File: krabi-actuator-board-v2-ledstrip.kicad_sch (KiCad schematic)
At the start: 0 parts

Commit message: adding LED strip
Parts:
- added LS1, LS2: Conn_01x02_Pin, symbol Connector:Conn_01x02_Pin
- added Q_LS1, Q_LS2: Q_NPN_BCE, symbol Device:Q_NPN_BCE
- added RB_LS1, RB_LS2: 1.2k, Resistor_SMD:R_0805_2012Metric, symbol Device:R
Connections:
- new net: LS2.1 (Pin_1), Q_LS2.2 (C)
- new net: Q_LS1.1 (B), RB_LS1.2
- new net: Q_LS2.1 (B), RB_LS2.2
- new net: LS1.1 (Pin_1), Q_LS1.2 (C)
- new net 12V: LS1.2 (Pin_2), LS2.2 (Pin_2)
- new net GND: Q_LS1.3 (E), Q_LS2.3 (E)
- new net LEDS_1: RB_LS1.1
- new net LEDS_2: RB_LS2.1
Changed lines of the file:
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@@
 (kicad_sch (version 20230121) (generator eeschema)
   (paper "A4")
+  (wire (pts (xy 53.34 45.72) (xy 57.15 45.72))
+    (stroke (width 0) (type default))
+  )
+  (wire (pts (xy 82.55 35.56) (xy 82.55 40.64))
+    (stroke (width 0) (type default))
+  )
+  (wire (pts (xy 85.09 77.47) (xy 85.09 82.55))
+    (stroke (width 0) (type default))
+  )
+  (wire (pts (xy 78.74 29.21) (xy 78.74 33.02))
+    (stroke (width 0) (type default))
+  )
+  (wire (pts (xy 85.09 74.93) (xy 81.28 74.93))
+    (stroke (width 0) (type default))
+  )
+  (wire (pts (xy 85.09 92.71) (xy 85.09 96.52))
+    (stroke (width 0) (type default))
+  )
+  (wire (pts (xy 67.31 87.63) (xy 77.47 87.63))
+    (stroke (width 0) (type default))
+  )
+  (wire (pts (xy 55.88 87.63) (xy 59.69 87.63))
+    (stroke (width 0) (type default))
+  )
+  (wire (pts (xy 64.77 45.72) (xy 74.93 45.72))
+    (stroke (width 0) (type default))
+  )
+  (wire (pts (xy 81.28 71.12) (xy 81.28 74.93))
+    (stroke (width 0) (type default))
+  )
+  (wire (pts (xy 82.55 50.8) (xy 82.55 54.61))
+    (stroke (width 0) (type default))
+  )
+  (wire (pts (xy 82.55 33.02) (xy 78.74 33.02))
+    (stroke (width 0) (type default))
+  )
+  (global_label "GND" (shape input) (at 82.55 54.61 270) (fields_autoplaced)
+    (effects (font (size 1.27 1.27)) (justify right))
+    (property "Intersheetrefs" "${INTERSHEET_REFS}" (at 82.55 61.5608 90)
+      (effects (font (size 1.27 1.27)) (justify right) hide)
+    )
+  )
+  (global_label "12V" (shape input) (at 78.74 29.21 90) (fields_autoplaced)
+    (effects (font (size 1.27 1.27)) (justify left))
+    (property "Intersheetrefs" "${INTERSHEET_REFS}" (at 78.74 22.6221 90)
+      (effects (font (size 1.27 1.27)) (justify left) hide)
+    )
+  )
+  (global_label "LEDS_2" (shape input) (at 55.88 87.63 180) (fields_autoplaced)
+    (effects (font (size 1.27 1.27)) (justify right))
+    (property "Intersheetrefs" "${INTERSHEET_REFS}" (at 45.966 87.63 0)
+      (effects (font (size 1.27 1.27)) (justify right) hide)
+    )
+  )
+  (global_label "LEDS_1" (shape input) (at 53.34 45.72 180) (fields_autoplaced)
+    (effects (font (size 1.27 1.27)) (justify right))
+    (property "Intersheetrefs" "${INTERSHEET_REFS}" (at 43.426 45.72 0)
+      (effects (font (size 1.27 1.27)) (justify right) hide)
+    )
+  )
+  (global_label "GND" (shape input) (at 85.09 96.52 270) (fields_autoplaced)
+    (effects (font (size 1.27 1.27)) (justify right))
+    (property "Intersheetrefs" "${INTERSHEET_REFS}" (at 85.09 103.4708 90)
+      (effects (font (size 1.27 1.27)) (justify right) hide)
+    )
+  )
+  (global_label "12V" (shape input) (at 81.28 71.12 90) (fields_autoplaced)
+    (effects (font (size 1.27 1.27)) (justify left))
+    (property "Intersheetrefs" "${INTERSHEET_REFS}" (at 81.28 64.5321 90)
+      (effects (font (size 1.27 1.27)) (justify left) hide)
+    )
+  )
+  (symbol (lib_id "Connector:Conn_01x02_Pin") (at 90.17 77.47 180) (unit 1)
+    (in_bom yes) (on_board yes) (dnp no) (fields_autoplaced)
+    (property "Reference" "LS2" (at 91.44 74.93 0)
+      (effects (font (size 1.27 1.27)) (justify right))
+    )
+    (property "Value" "Conn_01x02_Pin" (at 91.44 77.47 0)
+      (effects (font (size 1.27 1.27)) (justify right))
+    )
+    (property "Footprint" "" (at 90.17 77.47 0)
+      (effects (font (size 1.27 1.27)) hide)
+    )
+    (property "Datasheet" "~" (at 90.17 77.47 0)
+      (effects (font (size 1.27 1.27)) hide)
+    )
+    (property "Sim.Enable" "0" (at 90.17 77.47 0)
+      (effects (font (size 1.27 1.27)) hide)
+    )
+    (pin "1")
+    (pin "2")
+    (instances
+      (project "krabi-actuator-board-v2"
+        (path "/e63e39d7-6ac0-4ffd-8aa3-1841a4541b55/55fd7014-48ef-4cf3-914d-288b69fed1ef"
+          (reference "LS2") (unit 1)
+        )
+      )
+    )
+  )
+  (symbol (lib_id "Device:R") (at 60.96 45.72 90) (unit 1)
+    (in_bom yes) (on_board yes) (dnp no) (fields_autoplaced)
+    (property "Reference" "RB_LS1" (at 60.96 39.37 90)
+      (effects (font (size 1.27 1.27)))
+    )
+    (property "Value" "1.2k" (at 60.96 41.91 90)
+      (effects (font (size 1.27 1.27)))
+    )
+    (property "Footprint" "Resistor_SMD:R_0805_2012Metric" (at 60.96 47.498 90)
+      (effects (font (size 1.27 1.27)))
+    )
+    (property "Datasheet" "~" (at 60.96 45.72 0)
+      (effects (font (size 1.27 1.27)) hide)
+    )
+    (pin "1")
+    (pin "2")
+    (instances
+      (project "krabi-actuator-board-v2"
+        (path "/e63e39d7-6ac0-4ffd-8aa3-1841a4541b55/55fd7014-48ef-4cf3-914d-288b69fed1ef"
+          (reference "RB_LS1") (unit 1)
+        )
+      )
+    )
+  )
+  (symbol (lib_id "Device:Q_NPN_BCE") (at 82.55 87.63 0) (unit 1)
+    (in_bom yes) (on_board yes) (dnp no) (fields_autoplaced)
+    (property "Reference" "Q_LS2" (at 87.63 86.36 0)
+      (effects (font (size 1.27 1.27)) (justify left))
+    )
+    (property "Value" "Q_NPN_BCE" (at 87.63 88.9 0)
+      (effects (font (size 1.27 1.27)) (justify left))
+    )
+    (property "Footprint" "" (at 87.63 85.09 0)
+      (effects (font (size 1.27 1.27)) hide)
+    )
+    (property "Datasheet" "~" (at 82.55 87.63 0)
+      (effects (font (size 1.27 1.27)) hide)
+    )
+    (property "Sim.Enable" "0" (at 82.55 87.63 0)
+      (effects (font (size 1.27 1.27)) hide)
+    )
+    (pin "1")
+    (pin "2")
+    (pin "3")
+    (instances
+      (project "krabi-actuator-board-v2"
+        (path "/e63e39d7-6ac0-4ffd-8aa3-1841a4541b55/55fd7014-48ef-4cf3-914d-288b69fed1ef"
+          (reference "Q_LS2") (unit 1)
+        )
+      )
+    )
+  )
+  (symbol (lib_id "Device:Q_NPN_BCE") (at 80.01 45.72 0) (unit 1)
+    (in_bom yes) (on_board yes) (dnp no) (fields_autoplaced)
+    (property "Reference" "Q_LS1" (at 85.09 44.45 0)
+      (effects (font (size 1.27 1.27)) (justify left))
+    )
+    (property "Value" "Q_NPN_BCE" (at 85.09 46.99 0)
+      (effects (font (size 1.27 1.27)) (justify left))
+    )
+    (property "Footprint" "" (at 85.09 43.18 0)
+      (effects (font (size 1.27 1.27)) hide)
+    )
+    (property "Datasheet" "~" (at 80.01 45.72 0)
+      (effects (font (size 1.27 1.27)) hide)
+    )
+    (property "Sim.Enable" "0" (at 80.01 45.72 0)
+      (effects (font (size 1.27 1.27)) hide)
+    )
+    (pin "1")
+    (pin "2")
+    (pin "3")
+    (instances
+      (project "krabi-actuator-board-v2"
+        (path "/e63e39d7-6ac0-4ffd-8aa3-1841a4541b55/55fd7014-48ef-4cf3-914d-288b69fed1ef"
+          (reference "Q_LS1") (unit 1)
+        )
+      )
+    )
+  )
+  (symbol (lib_id "Device:R") (at 63.5 87.63 90) (unit 1)
+    (in_bom yes) (on_board yes) (dnp no) (fields_autoplaced)
+    (property "Reference" "RB_LS2" (at 63.5 81.28 90)
+      (effects (font (size 1.27 1.27)))
+    )
+    (property "Value" "1.2k" (at 63.5 83.82 90)
+      (effects (font (size 1.27 1.27)))
+    )
+    (property "Footprint" "Resistor_SMD:R_0805_2012Metric" (at 63.5 89.408 90)
+      (effects (font (size 1.27 1.27)))
+    )
+    (property "Datasheet" "~" (at 63.5 87.63 0)
+      (effects (font (size 1.27 1.27)) hide)
+    )
+    (pin "1")
+    (pin "2")
+    (instances
+      (project "krabi-actuator-board-v2"
+        (path "/e63e39d7-6ac0-4ffd-8aa3-1841a4541b55/55fd7014-48ef-4cf3-914d-288b69fed1ef"
+          (reference "RB_LS2") (unit 1)
+        )
+      )
+    )
+  )
+  (symbol (lib_id "Connector:Conn_01x02_Pin") (at 87.63 35.56 180) (unit 1)
+    (in_bom yes) (on_board yes) (dnp no) (fields_autoplaced)
+    (property "Reference" "LS1" (at 88.9 33.02 0)
+      (effects (font (size 1.27 1.27)) (justify right))
+    )
+    (property "Value" "Conn_01x02_Pin" (at 88.9 35.56 0)
+      (effects (font (size 1.27 1.27)) (justify right))
+    )
+    (property "Footprint" "" (at 87.63 35.56 0)
+      (effects (font (size 1.27 1.27)) hide)
+    )
+    (property "Datasheet" "~" (at 87.63 35.56 0)
+      (effects (font (size 1.27 1.27)) hide)
+    )
+    (property "Sim.Enable" "0" (at 87.63 35.56 0)
+      (effects (font (size 1.27 1.27)) hide)
+    )
+    (pin "1")
+    (pin "2")
+    (instances
+      (project "krabi-actuator-board-v2"
+        (path "/e63e39d7-6ac0-4ffd-8aa3-1841a4541b55/55fd7014-48ef-4cf3-914d-288b69fed1ef"
+          (reference "LS1") (unit 1)
+        )
+      )
+    )
+  )
 )

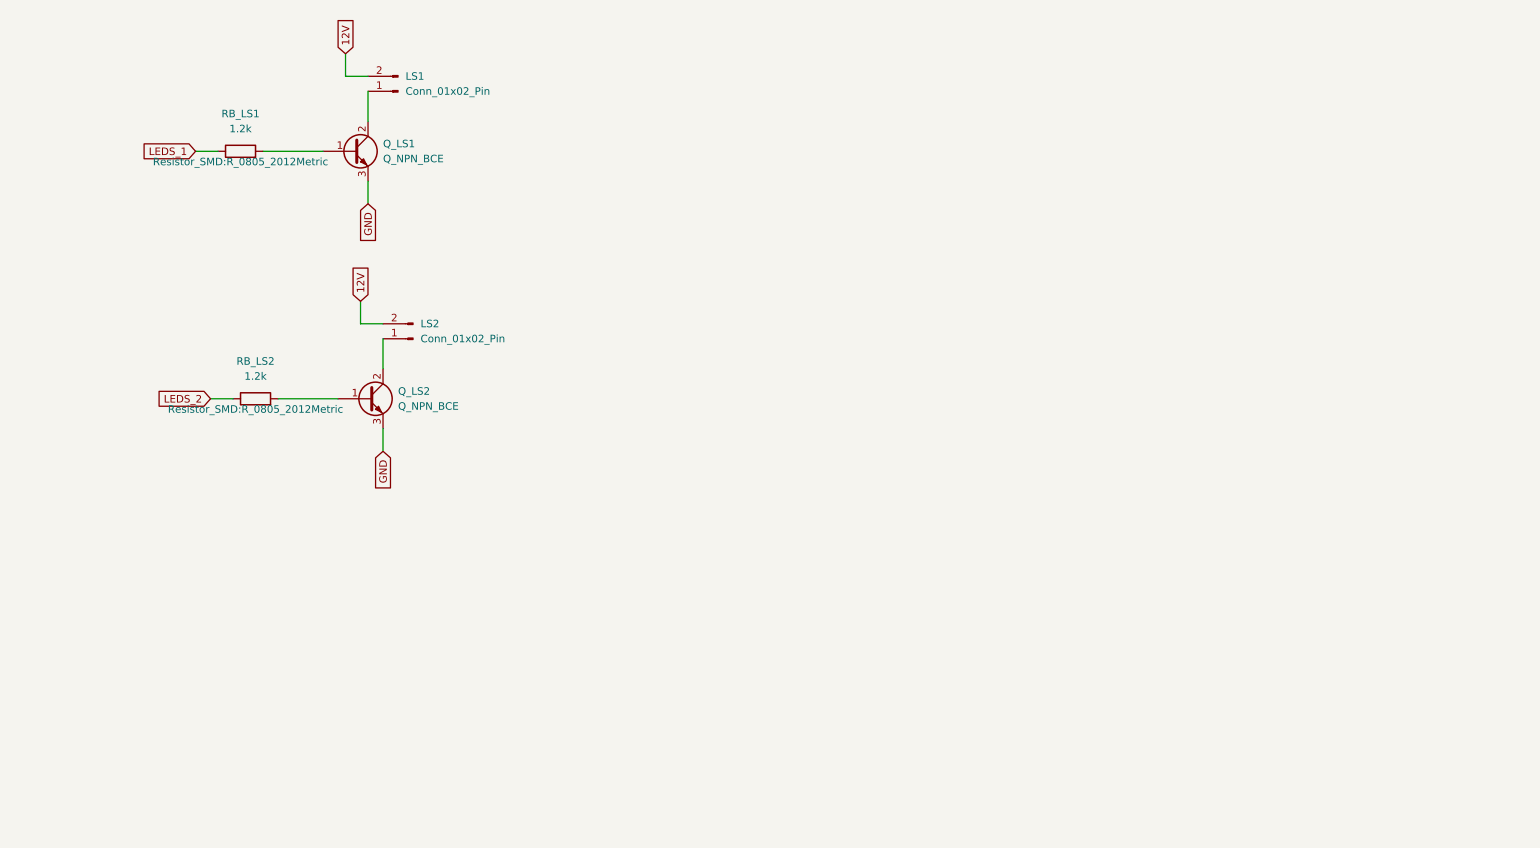
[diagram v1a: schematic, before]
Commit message: Add 2 led strip & led visualisation on all outputs
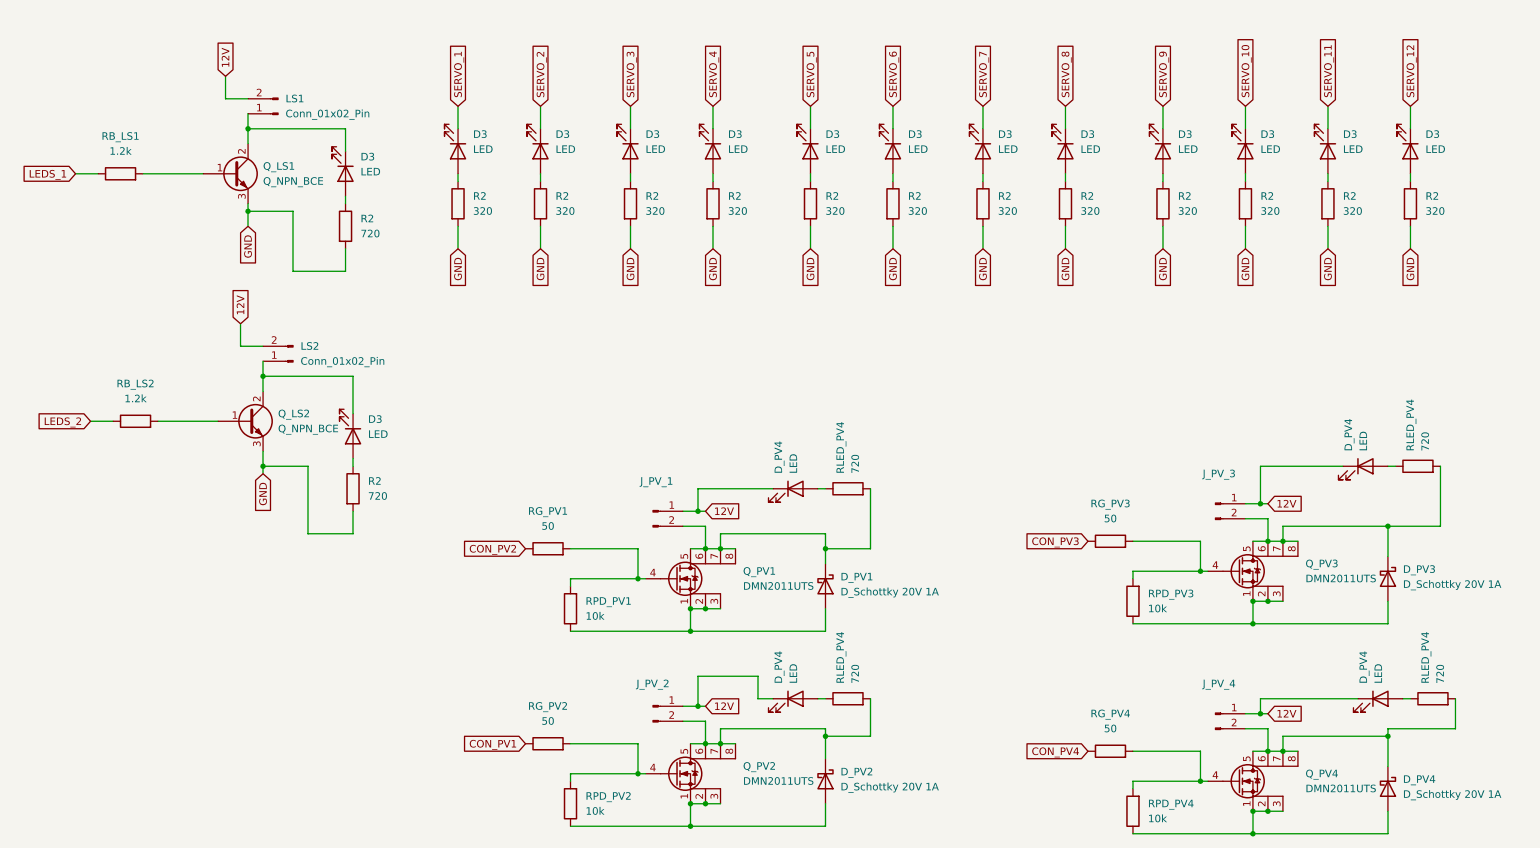
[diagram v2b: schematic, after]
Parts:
- added D3 (x14), D_PV4 (x4): LED, LED_SMD:LED_0805_2012Metric, symbol Device:LED
- added D_PV1, D_PV2, D_PV3, D_PV4: D_Schottky 20V 1A, symbol Device:D_Schottky
- added J_PV_1, J_PV_2, J_PV_3, J_PV_4: ~, symbol Connector:Conn_01x02_Pin
- added Q_PV1, Q_PV2, Q_PV3, Q_PV4: DMN2011UTS, Package_SO:TSSOP-8_4.4x3mm_P0.65mm, symbol Krabi:DMN2011UTS
- added R2 (x12): 320, Resistor_SMD:R_0805_2012Metric, symbol Device:R
- added R2 (x2), RLED_PV4 (x4): 720, Resistor_SMD:R_0805_2012Metric, symbol Device:R
- added RG_PV1, RG_PV2, RG_PV3, RG_PV4: 50, symbol Device:R
- added RPD_PV1, RPD_PV2, RPD_PV3, RPD_PV4: 10k, symbol Device:R
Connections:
- net 12V: now also D_PV4.1 (K), D_PV4.1 (K), D_PV4.1 (K), D_PV4.1 (K), J_PV_1.1 (Pin_1), J_PV_2.1 (Pin_1), J_PV_3.1 (Pin_1), J_PV_4.1 (Pin_1)
- net GND: now also R2.2, R2.2, R2.2, R2.2, R2.2, R2.2, R2.2, R2.2, R2.2, R2.2, R2.2, R2.2, R2.2, R2.2
- net at LS2.1 (Pin_1), Q_LS2.2 (C): now also D3.1 (K)
- net at LS1.1 (Pin_1), Q_LS1.2 (C): now also D3.1 (K)
- new net: D_PV1.1 (K), J_PV_1.2 (Pin_2), Q_PV1.5 (D), Q_PV1.6 (D), Q_PV1.7 (D), Q_PV1.8 (D), RLED_PV4.2
- new net: D3.2 (A), R2.1 (x14)
- new net: D_PV1.2 (A), Q_PV1.1 (S), Q_PV1.2 (S), Q_PV1.3 (S), RPD_PV1.1
- new net: Q_PV1.4 (G), RG_PV1.2, RPD_PV1.2
- new net: D_PV4.2 (A), RLED_PV4.1 (x4)
- new net: D_PV4.1 (K), J_PV_4.2 (Pin_2), Q_PV4.5 (D), Q_PV4.6 (D), Q_PV4.7 (D), Q_PV4.8 (D), RLED_PV4.2
- new net: D_PV2.2 (A), Q_PV2.1 (S), Q_PV2.2 (S), Q_PV2.3 (S), RPD_PV2.1
- new net: Q_PV2.4 (G), RG_PV2.2, RPD_PV2.2
- new net: D_PV3.1 (K), J_PV_3.2 (Pin_2), Q_PV3.5 (D), Q_PV3.6 (D), Q_PV3.7 (D), Q_PV3.8 (D), RLED_PV4.2
- new net: D_PV3.2 (A), Q_PV3.1 (S), Q_PV3.2 (S), Q_PV3.3 (S), RPD_PV3.1
- new net: Q_PV3.4 (G), RG_PV3.2, RPD_PV3.2
- new net: D_PV2.1 (K), J_PV_2.2 (Pin_2), Q_PV2.5 (D), Q_PV2.6 (D), Q_PV2.7 (D), Q_PV2.8 (D), RLED_PV4.2
- new net: Q_PV4.4 (G), RG_PV4.2, RPD_PV4.2
- new net: D_PV4.2 (A), Q_PV4.1 (S), Q_PV4.2 (S), Q_PV4.3 (S), RPD_PV4.1
- new net CON_PV1: RG_PV2.1
- new net CON_PV2: RG_PV1.1
- new net CON_PV3: RG_PV3.1
- new net CON_PV4: RG_PV4.1
- new net SERVO_1: D3.1 (K)
- new net SERVO_10: D3.1 (K)
- new net SERVO_11: D3.1 (K)
- new net SERVO_12: D3.1 (K)
- new net SERVO_2: D3.1 (K)
- new net SERVO_3: D3.1 (K)
- new net SERVO_4: D3.1 (K)
- new net SERVO_5: D3.1 (K)
- new net SERVO_6: D3.1 (K)
- new net SERVO_7: D3.1 (K)
- new net SERVO_8: D3.1 (K)
- new net SERVO_9: D3.1 (K)
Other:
- moved on the sheet: LS1, LS2, Q_LS1, Q_LS2, RB_LS1, RB_LS2

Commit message: Assigning footprints to schemas
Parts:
- D_PV1, D_PV2, D_PV3, D_PV4: footprint (none) -> Diode_SMD:D_SMA
- J_PV_1, J_PV_2, J_PV_3, J_PV_4, LS1, LS2: footprint (none) -> Connector_JST:JST_PH_B2B-PH-K_1x02_P2.00mm_Vertical
- Q_LS1, Q_LS2: value Q_NPN_BCE -> DMN2011UTS; footprint (none) -> Package_SO:TSSOP-8_4.4x3mm_P0.65mm; symbol Device:Q_NPN_BCE -> Krabi:DMN2011UTS
- RG_PV1, RG_PV2, RG_PV3, RG_PV4, RPD_PV1, RPD_PV2, RPD_PV3, RPD_PV4: footprint (none) -> Resistor_SMD:R_0805_2012Metric
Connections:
- net GND: now also Q_LS1.1 (S), Q_LS2.1 (S); no longer Q_LS1.3 (E), Q_LS2.3 (E)
- net at D3.1 (K), LS2.1 (Pin_1): now also Q_LS2.5 (D); no longer Q_LS2.2 (C)
- net at RB_LS1.2: now also Q_LS1.4 (G); no longer Q_LS1.1 (B)
- net at RB_LS2.2: now also Q_LS2.4 (G); no longer Q_LS2.1 (B)
- net at D3.1 (K), LS1.1 (Pin_1): now also Q_LS1.5 (D); no longer Q_LS1.2 (C)
